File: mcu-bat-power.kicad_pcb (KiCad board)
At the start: 2 copper layers, 2 parts

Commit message: First version with all components set and placed
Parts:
- removed the G*** at (30.5, 184.9)
- added BT1: BH-18650-B1BA002, Chof747 Footprints:BH18650B1BA002, F.Cu at (60.6, 105.5)
- added C1: 1uF, Capacitor_SMD:C_0603_1608Metric_Pad1.08x0.95mm_HandSolder, F.Cu at (79.1, 136.7)
- added C2: 0.1uF, Capacitor_SMD:C_0603_1608Metric_Pad1.08x0.95mm_HandSolder, F.Cu at (73.9, 124.5)
- added C3: 22uF, Capacitor_SMD:C_0603_1608Metric_Pad1.08x0.95mm_HandSolder, F.Cu at (76.2, 84.6)
- added C4: 4u7, Capacitor_SMD:C_0603_1608Metric_Pad1.08x0.95mm_HandSolder, F.Cu at (83.3, 136.8)
- added C5: 22uF, Capacitor_SMD:C_0603_1608Metric_Pad1.08x0.95mm_HandSolder, F.Cu at (82.9, 84.6)
- added D1: RED, LED_SMD:LED_0603_1608Metric_Pad1.05x0.95mm_HandSolder, F.Cu at (75.0, 99.0)
- added D2: GREEN, LED_SMD:LED_0603_1608Metric_Pad1.05x0.95mm_HandSolder, F.Cu at (75.1, 105.3)
- added D3: SS34A, Chof747 Footprints:DIOM5026X262N, F.Cu at (85.4, 86.5)
- added IC1: CN3058E, Chof747 Footprints:SOIC127P600X175-9N, F.Cu at (81.2, 133.1)
- added IC2: HY2112, Chof747 Footprints:SOT95P280X145-6N, F.Cu at (77.0, 122.6)
- added J1: USB_B_Micro, Chof747 Footprints:Micro USB, F.Cu at (77.1, 147.1)
- added J2: INDICATORS, Connector_PinHeader_2.54mm:PinHeader_1x04_P2.54mm_Horizontal, F.Cu at (85.9, 99.4)
- added J3: PWR, Connector_PinHeader_2.54mm:PinHeader_1x02_P2.54mm_Horizontal, F.Cu at (85.9, 74.1)
- added J4: USB, Connector_PinHeader_2.54mm:PinHeader_1x02_P2.54mm_Horizontal, F.Cu at (85.9, 144.9)
- added L1: 22uH, Chof747 Footprints:SMD0740, F.Cu at (79.6, 90.2)
- added Q1: FS8205, Chof747 Footprints:FS8205, F.Cu at (76.3, 118.2)
- added Q2: 2N7002, Package_TO_SOT_SMD:SOT-23, F.Cu at (79.4, 105.2)
- added Q3: 2N7002, Package_TO_SOT_SMD:SOT-23, F.Cu at (79.5, 99.0)
- added R1: 1k, Resistor_SMD:R_0603_1608Metric_Pad0.98x0.95mm_HandSolder, F.Cu at (74.1, 102.2)
- added R10: 100, Resistor_SMD:R_0603_1608Metric_Pad0.98x0.95mm_HandSolder, F.Cu at (76.7, 125.2)
- added R11: 7k5, Resistor_SMD:R_0603_1608Metric_Pad0.98x0.95mm_HandSolder, F.Cu at (81.9, 82.0)
- added R12: 1k, Resistor_SMD:R_0603_1608Metric_Pad0.98x0.95mm_HandSolder, F.Cu at (81.9, 80.5)
- added R13: 2k, Resistor_SMD:R_0603_1608Metric_Pad0.98x0.95mm_HandSolder, F.Cu at (80.1, 123.5)
- added R2: 0, Resistor_SMD:R_0603_1608Metric_Pad0.98x0.95mm_HandSolder, F.Cu at (86.4, 131.5)
- added R3: 2k4 / 1k2, Resistor_SMD:R_0603_1608Metric_Pad0.98x0.95mm_HandSolder, F.Cu at (75.1, 131.5)
- added R4: 10k, Resistor_SMD:R_0603_1608Metric_Pad0.98x0.95mm_HandSolder, F.Cu at (76.9, 105.2)
- added R5: 470k, Resistor_SMD:R_0603_1608Metric_Pad0.98x0.95mm_HandSolder, F.Cu at (83.4, 111.1)
- added R6: 470k, Resistor_SMD:R_0603_1608Metric_Pad0.98x0.95mm_HandSolder, F.Cu at (85.0, 111.1)
- added R7: 10k, Resistor_SMD:R_0603_1608Metric_Pad0.98x0.95mm_HandSolder, F.Cu at (76.9, 99.0)
- added R8: 10k, Resistor_SMD:R_0603_1608Metric_Pad0.98x0.95mm_HandSolder, F.Cu at (82.3, 99.1)
- added R9: 10k, Resistor_SMD:R_0603_1608Metric_Pad0.98x0.95mm_HandSolder, F.Cu at (82.3, 105.2)
- added SW1: SW_SPDT, Chof747 Footprints:Slide-switch-SS-12D11L7, F.Cu at (81.0, 65.5)
- added U1: MT3608, Package_TO_SOT_SMD:SOT-23-6, F.Cu at (79.2, 84.6)
- moved G*** 114.0 mm to (60.6, 74.9), turned to -90 degrees
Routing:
- net BAT+: track 0.00 -> 113.0 mm
- net VBUS: track 0.00 -> 73.4 mm, vias 0 -> 3
- net VBAT: track 0.00 -> 72.4 mm
- net BAT-: track 0.00 -> 46.2 mm, vias 0 -> 2
- net CHG_IND: track 0.00 -> 42.5 mm, vias 0 -> 2
- net RDY_IND: track 0.00 -> 37.2 mm, vias 0 -> 2
- net +5V: track 0.00 -> 19.5 mm
- net Net-(J2-Pin_2): track 0.00 -> 13.8 mm
- net USB_P: track 0.00 -> 13.1 mm
- net USB_N: track 0.00 -> 13.0 mm
- net GND: track 0.00 -> 12.2 mm, vias 0 -> 14
- net /boosted: track 0.00 -> 8.78 mm
- net VREF: track 0.00 -> 8.23 mm
- net Net-(J2-Pin_3): track 0.00 -> 8.00 mm
- net Net-(IC2-OC): track 0.00 -> 6.48 mm
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- added copper zone on F.Cu, net BAT+
- added copper zone on B.Cu, net GND
- added copper zone on F.Cu, net GND
- added copper zone on F.Cu, net VBAT
- added copper zone on F.Cu, net VBUS
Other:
- board outline added: 41 x 90.9 mm
- board text added: "Charging"
- board text added: "Ready"

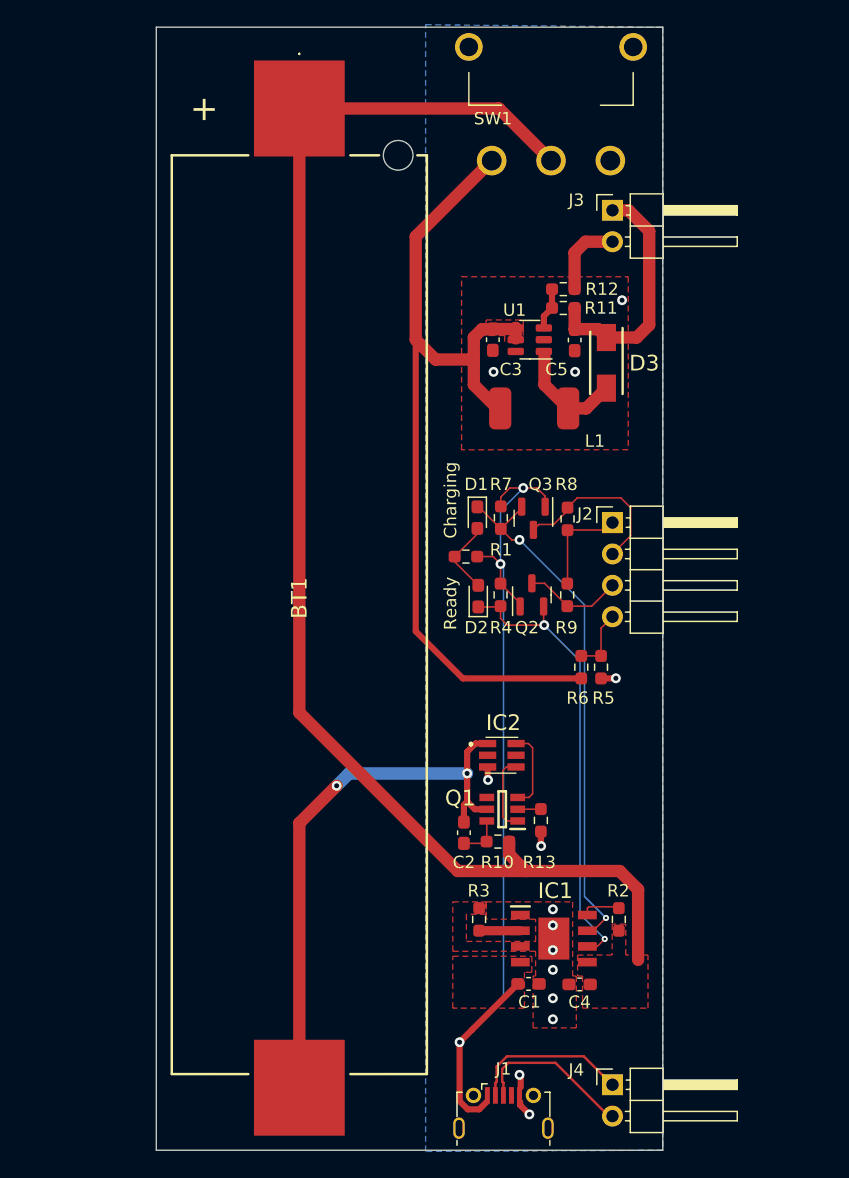
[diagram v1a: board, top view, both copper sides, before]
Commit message: running dcr checks and excluding unnecessary issues
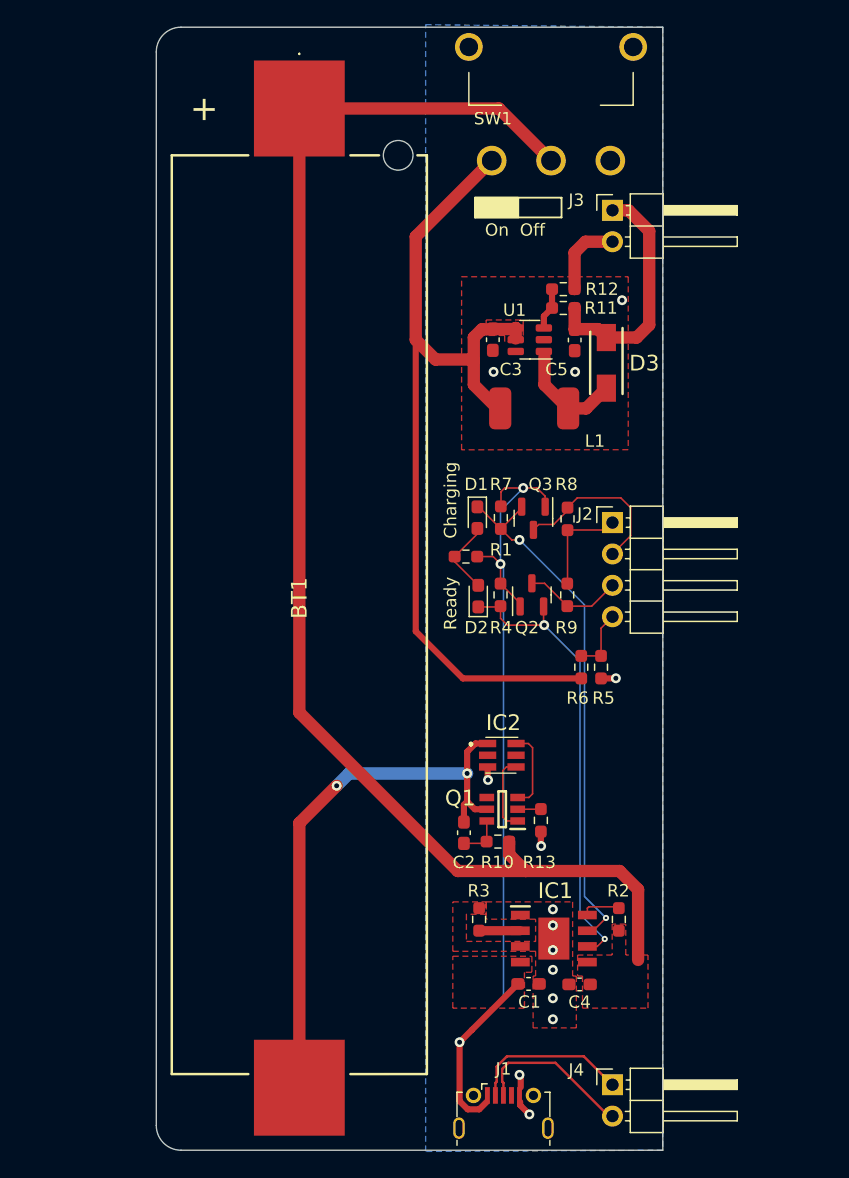
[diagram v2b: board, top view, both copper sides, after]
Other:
- outline, holes or cut-outs redrawn
- board text added: "+5V"
- board text added: "BAT V Sense (VBAT / 2)"
- board text added: "Battery Power Board (LiFePo4) v1.0 (2023)"
- board text added: "CHG IND"
- board text added: "D+"
- board text added: "D-"
- board text added: "GND"
- board text added: "On Off"
- board text added: "RDY IND"
- board text added: "USB"
- board text added: "VREF (=MCU Voltage)"
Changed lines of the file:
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@@
     (pad "2" smd rect (at -39.63 0 180) (size 7.35 7.77) (layers "F.Cu" "F.Paste" "F.Mask")
       (net 2 "BAT-") (pinfunction "-") (pintype "passive"))
-    (model "BH-18650-B1BA002.stp"
+    (model "${USERMODELS}/3dmodels/BH-18650-B1BA002.stp"
       (offset (xyz 0 0 0))
       (scale (xyz 1 1 1))
@@
     (pad "9" smd rect (at 0 0) (size 2.513 3.402) (layers "F.Cu" "F.Paste" "F.Mask")
       (net 4 "GND") (pinfunction "EP") (pintype "passive"))
-    (model "TP4056-42-ESOP8.stp"
+    (model "${USERMODELS}/3dmodels/CN3058E.stp"
       (offset (xyz 0 0 0))
       (scale (xyz 1 1 1))
@@
     (pad "2" smd roundrect (at 2.75 0) (size 1.8 3.4) (layers "F.Cu" "F.Paste" "F.Mask") (roundrect_rratio 0.25)
       (net 20 "/boosted") (pinfunction "2") (pintype "passive") (thermal_bridge_angle 45))
+    (model "${USERMODELS}/3dmodels/YSPI0740.step"
+      (offset (xyz -3.7 3.3 0))
+      (scale (xyz 1 1 1))
+      (rotate (xyz -90 0 0))
+    )
   )
   (footprint "Resistor_SMD:R_0603_1608Metric_Pad0.98x0.95mm_HandSolder" (layer "F.Cu")
@@
     (pad "6" thru_hole oval (at 3.6 1.3) (size 0.94 1.75) (drill oval 0.55 1.35) (layers "*.Cu" "*.Mask")
       (net 28 "unconnected-(J1-Shield-Pad6)") (pinfunction "Shield") (pintype "passive+no_connect"))
-    (model "${KICAD6_3DMODEL_DIR}/Connector_USB.3dshapes/USB_Micro-B_Amphenol_10118194_Horizontal.wrl"
-      (offset (xyz 0 0 0))
-      (scale (xyz 1 1 1))
+    (model "${USERMODELS}/3dmodels/usb-micro-conn.wrl"
+      (offset (xyz 0 0 1.2))
+      (scale (xyz 0.3 0.3 0.3))
       (rotate (xyz 0 0 0))
     )
@@
     (property "ki_description" "MULTICOMP - SS34A - DIODE, RECTIFIER, 3A, 40V, DO-214AC")
     (attr smd)
-    (fp_text reference "D3" (at 0.03 -3.07 -180) (layer "F.SilkS")
+    (fp_text reference "D3" (at 0.03 -3.07) (layer "F.SilkS")
         (effects (font (size 1.27 1.27) (thickness 0.254)))
     )
@@
     (pad "2" smd rect (at 2.05 0) (size 1.55 2.2) (layers "F.Cu" "F.Paste" "F.Mask")
       (net 20 "/boosted") (pinfunction "A") (pintype "passive"))
-    (model "SS34A.stp"
+    (model "${USERMODELS}/3dmodels/SS34A.stp"
       (offset (xyz 0 0 0))
       (scale (xyz 1 1 1))
@@
     (pad "4" thru_hole circle (at 6.65 -4.6) (size 2.25 2.25) (drill 1.5) (layers "*.Cu" "*.Mask"))
     (pad "5" thru_hole circle (at -6.65 -4.6) (size 2.25 2.25) (drill 1.5) (layers "*.Cu" "*.Mask"))
+    (model "${USERMODELS}/3dmodels/SS-12D11L7.stp"
+      (offset (xyz 0 3 3.3))
+      (scale (xyz 1 1 1))
+      (rotate (xyz 0 180 0))
+    )
   )
   (footprint "Package_TO_SOT_SMD:SOT-23-6" (layer "F.Cu")
@@
       (stroke (width 0) (type solid)) (fill solid) (layer "B.SilkS"))
   )
-  (gr_rect (start 49 59.3) (end 90 150.2)
-    (stroke (width 0.1) (type default)) (fill none) (layer "Edge.Cuts"))
+  (gr_rect (start 74.8 73.1) (end 78.3 74.7)
+    (stroke (width 0.15) (type solid)) (fill solid) (layer "F.SilkS"))
+  (gr_rect (start 74.8 73.1) (end 81.8 74.7)
+    (stroke (width 0.15) (type default)) (fill none) (layer "F.SilkS"))
+  (gr_arc (start 51 150.2) (mid 49.585786 149.614214) (end 49 148.2)
+    (stroke (width 0.1) (type default)) (layer "Edge.Cuts"))
+  (gr_arc (start 49 61.3) (mid 49.585786 59.885786) (end 51 59.3)
+    (stroke (width 0.1) (type default)) (layer "Edge.Cuts"))
+  (gr_line (start 90 150.2) (end 51 150.2)
+    (stroke (width 0.1) (type default)) (layer "Edge.Cuts"))
+  (gr_line (start 90 59.3) (end 90 150.2)
+    (stroke (width 0.1) (type default)) (layer "Edge.Cuts"))
+  (gr_line (start 51 59.3) (end 90 59.3)
+    (stroke (width 0.1) (type default)) (layer "Edge.Cuts"))
+  (gr_line (start 49 148.2) (end 49 61.3)
+    (stroke (width 0.1) (type default)) (layer "Edge.Cuts"))
+  (gr_text "USB" (at 87.4 143.6) (layer "B.SilkS")
+    (effects (font (size 1 1) (thickness 0.15)) (justify left bottom mirror))
+  )
+  (gr_text "+5V" (at 84.4 74.6) (layer "B.SilkS")
+    (effects (font (size 1 1) (thickness 0.15)) (justify left bottom mirror))
+  )
+  (gr_text "CHG IND" (at 84.5 102.5) (layer "B.SilkS")
+    (effects (font (size 1 1) (thickness 0.15)) (justify left bottom mirror))
+  )
+  (gr_text "GND" (at 84.4 77.1) (layer "B.SilkS")
+    (effects (font (size 1 1) (thickness 0.15)) (justify left bottom mirror))
+  )
+  (gr_text "RDY IND" (at 84.4 105.1) (layer "B.SilkS")
+    (effects (font (size 1 1) (thickness 0.15)) (justify left bottom mirror))
+  )
+  (gr_text "D+" (at 84.6 147.9) (layer "B.SilkS")
+    (effects (font (size 1 1) (thickness 0.15)) (justify left bottom mirror))
+  )
+  (gr_text "D-" (at 84.6 145.5) (layer "B.SilkS")
+    (effects (font (size 1 1) (thickness 0.15)) (justify left bottom mirror))
+  )
+  (gr_text "VREF (=MCU Voltage)" (at 84.5 100) (layer "B.SilkS")
+    (effects (font (size 1 1) (thickness 0.15)) (justify left bottom mirror))
+  )
+  (gr_text "BAT V Sense (VBAT / 2)" (at 84.3 107.5) (layer "B.SilkS")
+    (effects (font (size 1 1) (thickness 0.15)) (justify left bottom mirror))
+  )
+  (gr_text "Battery Power Board (LiFePo4)\nv1.0 (2023)" (at 57.9 78.9 90) (layer "B.SilkS")
+    (effects (font (size 2 2) (thickness 0.3)) (justify left bottom mirror))
+  )
   (gr_text "Ready" (at 73.4 108.1 90) (layer "F.SilkS")
     (effects (font (size 1 1) (thickness 0.15)) (justify left bottom))
@@
     (effects (font (size 1 1) (thickness 0.15)) (justify left bottom))
   )
+  (gr_text "On  Off" (at 75.6 76.3) (layer "F.SilkS")
+    (effects (font (size 1 1) (thickness 0.15)) (justify left bottom))
+  )
   (segment (start 78.9 127.6) (end 73.4 127.6) (width 1) (layer "F.Cu") (net 1))
   (segment (start 88 129.1) (end 86.5 127.6) (width 1) (layer "F.Cu") (net 1))
@@
   (segment (start 64.6 119.7) (end 63.6 120.7) (width 1) (layer "B.Cu") (net 2))
   (segment (start 74.209009 146.89) (end 75.140991 146.89) (width 0.5) (layer "F.Cu") (net 3))
-  (segment (start 76.8875 98.0875) (end 76.8875 97.325) (width 0.13) (layer "F.Cu") (net 3))
-  (segment (start 77.6125 96.6) (end 78.7 96.6) (width 0.13) (layer "F.Cu") (net 3))
   (segment (start 80.475 98.1125) (end 80.475 97.2625) (width 0.13) (layer "F.Cu") (net 3))
   (segment (start 78.45 105.925) (end 76.8625 104.3375) (width 0.13) (layer "F.Cu") (net 3))
+  (segment (start 76.9 98.075) (end 76.8875 98.0875) (width 0.13) (layer "F.Cu") (net 3))
   (segment (start 73.55 146.230991) (end 74.209009 146.89) (width 0.5) (layer "F.Cu") (net 3))
   (segment (start 74.55375 140.45375) (end 73.55 141.4575) (width 0.5) (layer "F.Cu") (net 3))
+  (segment (start 76.9 96.9) (end 76.9 98.075) (width 0.13) (layer "F.Cu") (net 3))
   (segment (start 78.45 106.1875) (end 78.45 105.925) (width 0.13) (layer "F.Cu") (net 3))
-  (segment (start 76.8875 97.325) (end 77.6125 96.6) (width 0.13) (layer "F.Cu") (net 3))
+  (segment (start 77.2 96.6) (end 76.9 96.9) (width 0.13) (layer "F.Cu") (net 3))
   (segment (start 76.2625 102.15) (end 76.8625 102.75) (width 0.13) (layer "F.Cu") (net 3))
   (segment (start 73.55 141.4575) (end 73.55 146.230991) (width 0.5) (layer "F.Cu") (net 3))
@@
   (segment (start 76.8625 102.75) (end 76.8625 104.3375) (width 0.13) (layer "F.Cu") (net 3))
   (segment (start 78.2675 136.74) (end 74.55375 140.45375) (width 0.5) (layer "F.Cu") (net 3))
+  (segment (start 78.7 96.6) (end 77.2 96.6) (width 0.13) (layer "F.Cu") (net 3))
   (segment (start 80.475 97.2625) (end 79.8125 96.6) (width 0.13) (layer "F.Cu") (net 3))
   (segment (start 75.140991 146.89) (end 75.75 146.280991) (width 0.5) (layer "F.Cu") (net 3))

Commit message: Version 1.0 (sent to fabhouse) + updated readme
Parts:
- removed BT1: BH-18650-B1BA002, Chof747 Footprints:BH18650B1BA002
- removed the G*** at (60.6, 74.9)
- added BAT1: BH-18650-B1BA002, Chof747 Footprints:BH18650B1BA002, F.Cu at (51.0, 104.1)
- added D4: PWR, LED_SMD:LED_0603_1608Metric_Pad1.05x0.95mm_HandSolder, F.Cu at (78.5, 77.3)
- added D5: USB, LED_SMD:LED_0603_1608Metric_Pad1.05x0.95mm_HandSolder, F.Cu at (69.4, 147.2)
- added G***: LOGO, Chof747 Logos:LOGO small, B.Cu at (74.2, 104.6)
- added H1: MountingHole, Chof747 Footprints:MountingHole_3.2mm_M3-smallBorder, F.Cu at (42.5, 63.4)
- added H2: MountingHole, Chof747 Footprints:MountingHole_3.2mm_M3-smallBorder, F.Cu at (93.0, 63.4)
- added H3: MountingHole, Chof747 Footprints:MountingHole_3.2mm_M3-smallBorder, F.Cu at (42.5, 146.1)
- added H4: MountingHole, Chof747 Footprints:MountingHole_3.2mm_M3-smallBorder, F.Cu at (93.0, 146.1)
- added J5: PWR, Chof747_Connectors:pad_1x2_1.5mmx3mm, F.Cu at (86.1, 148.5)
- added JP1: A1_H, Jumper:SolderJumper-2_P1.3mm_Open_RoundedPad1.0x1.5mm, B.Cu at (66.6, 107.3)
- added JP2: A1_L, Jumper:SolderJumper-2_P1.3mm_Open_RoundedPad1.0x1.5mm, B.Cu at (66.6, 109.8)
- added JP3: A0_H, Jumper:SolderJumper-2_P1.3mm_Open_RoundedPad1.0x1.5mm, B.Cu at (66.6, 101.8)
- added JP4: A0_L, Jumper:SolderJumper-2_P1.3mm_Open_RoundedPad1.0x1.5mm, B.Cu at (66.6, 104.3)
- added NT1: NetTie_2, NetTie:NetTie-2_SMD_Pad0.5mm, F.Cu at (79.7, 144.0)
- added R14: 1k, Resistor_SMD:R_0603_1608Metric_Pad0.98x0.95mm_HandSolder, F.Cu at (65.4, 147.2)
- added TP1: GND, TestPoint:TestPoint_Pad_2.0x2.0mm, F.Cu at (64.8, 70.5)
- added TP10: CHG, TestPoint:TestPoint_Pad_2.0x2.0mm, F.Cu at (64.8, 106.0)
- added TP2: VBAT, TestPoint:TestPoint_Pad_2.0x2.0mm, F.Cu at (64.8, 74.5)
- added TP3: BAT+, TestPoint:TestPoint_Pad_2.0x2.0mm, F.Cu at (64.8, 78.5)
- added TP4: BAT-, TestPoint:TestPoint_Pad_2.0x2.0mm, F.Cu at (64.8, 82.6)
- added TP5: 5V, TestPoint:TestPoint_Pad_2.0x2.0mm, F.Cu at (64.9, 86.6)
- added TP6: FDBK, TestPoint:TestPoint_Pad_2.0x2.0mm, F.Cu at (64.8, 90.7)
- added TP7: VBUS, TestPoint:TestPoint_Pad_2.0x2.0mm, F.Cu at (64.8, 141.4)
- added TP8: VREF, TestPoint:TestPoint_Pad_2.0x2.0mm, F.Cu at (64.8, 114.1)
- added TP9: RDY, TestPoint:TestPoint_Pad_2.0x2.0mm, F.Cu at (64.8, 110.1)
- added U2: INA219AxD, Package_SO:SOIC-8_3.9x4.9mm_P1.27mm, F.Cu at (83.4, 99.5)
- C3, C5: footprint Capacitor_SMD:C_0603_1608Metric_Pad1.08x0.95mm_HandSolder -> Capacitor_SMD:C_1206_3216Metric_Pad1.33x1.80mm_HandSolder
- J2: footprint Connector_PinHeader_2.54mm:PinHeader_1x04_P2.54mm_Horizontal -> Connector_PinHeader_2.54mm:PinHeader_1x06_P2.54mm_Horizontal
- R5: value 470k -> 0R1; footprint Resistor_SMD:R_0603_1608Metric_Pad0.98x0.95mm_HandSolder -> Resistor_SMD:R_2512_6332Metric_Pad1.40x3.35mm_HandSolder
- R6: value 470k -> 1k
- moved R6 35.3 mm to (75.0, 77.3), turned to 0 degrees
- moved R5 14.4 mm to (76.1, 98.7), turned to 90 degrees
- moved J4 9.12 mm to (92.9, 139.1)
- moved J2 8.63 mm to (92.9, 104.5)
- moved Q1 8.31 mm to (83.6, 122.3), turned to -90 degrees
- moved Q3 8.19 mm to (79.7, 107.2)
- moved D2 7.96 mm to (75.1, 113.3)
- moved R8 7.96 mm to (82.3, 107.1)
- moved D1 7.96 mm to (75.0, 107.0)
- moved Q2 7.96 mm to (79.4, 113.2)
- moved R1 7.96 mm to (74.1, 110.1)
- moved R4 7.96 mm to (76.9, 113.2)
- moved R7 7.96 mm to (76.9, 107.0)
- moved R9 7.96 mm to (82.3, 113.2)
- moved J3 7.00 mm to (92.9, 74.1)
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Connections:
- net Net-(U1-FB) renamed FDBK
- C3 pad 1: VBAT -> VBAT_M
- J1 pad 6: unconnected-(J1-Shield-Pad6) -> Net-(J1-Shield)
- J2 pad 4: /BAT_SENSE -> SDA
- L1 pad 1: VBAT -> VBAT_M
- R5 pad 1: /BAT_SENSE -> VBAT
- R5 pad 2: VBAT -> VBAT_M
- R6 pad 1: GND -> VBAT
- R6 pad 2: /BAT_SENSE -> Net-(D4-A)
- U1 pad 4: VBAT -> VBAT_M
- U1 pad 5: VBAT -> VBAT_M
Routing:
- net VREF: track 8.23 -> 86.5 mm, vias 0 -> 1
- net GND: track 12.2 -> 69.5 mm, vias 14 -> 16
- net BAT-: track 46.2 -> 98.0 mm, vias 2 -> 3
- net +5V: track 19.5 -> 68.1 mm, vias 0 -> 4
- net BAT+: track 113.0 -> 146.7 mm
- net VBAT_M: track 0.00 -> 29.2 mm
- net SCL: track 0.00 -> 24.9 mm
- net Net-(JP1-A): track 0.00 -> 24.2 mm, vias 0 -> 3
- net Net-(JP3-A): track 0.00 -> 23.6 mm, vias 0 -> 3
- net SDA: track 0.00 -> 21.8 mm
- net VBUS: track 73.6 -> 95.0 mm, vias 3 -> 5
- net FDBK: track 3.41 -> 21.3 mm, vias 0 -> 2
- net Net-(J1-Shield): track 0.00 -> 15.5 mm
- net VBAT: track 72.4 -> 57.1 mm
- net Net-(J2-Pin_3): track 8.00 -> 16.2 mm
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- removed copper zone on F.Cu, net VBAT
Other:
- board size 41 x 90.9 mm -> 58.6 x 90.9 mm
- board text added: "Battery Power (LiFePo4) v1.0 (2024)"
- board text added: "INA219 Adr."
- board text added: "SCL(I2C)"
- board text added: "SDA(I2C)"
- board text added: "VBUS"
- board text added: "VREF"
- board text removed: "BAT V Sense (VBAT / 2)"
- board text removed: "Battery Power Board (LiFePo4) v1.0 (2023)"
- board text removed: "VREF (=MCU Voltage)"
